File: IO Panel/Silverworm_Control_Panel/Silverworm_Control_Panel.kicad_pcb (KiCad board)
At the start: 2 copper layers, 74 x 208.7 mm, 32 parts, among them J1 Microfit 6-pin, J2 Conn_01x15, J3 Conn_01x15, J4 JST-PH-2PIN, J5 JST-PH-2PIN, J6 JST-PH-2PIN, J7 JST-PH-2PIN, SW1 SW_SPDT

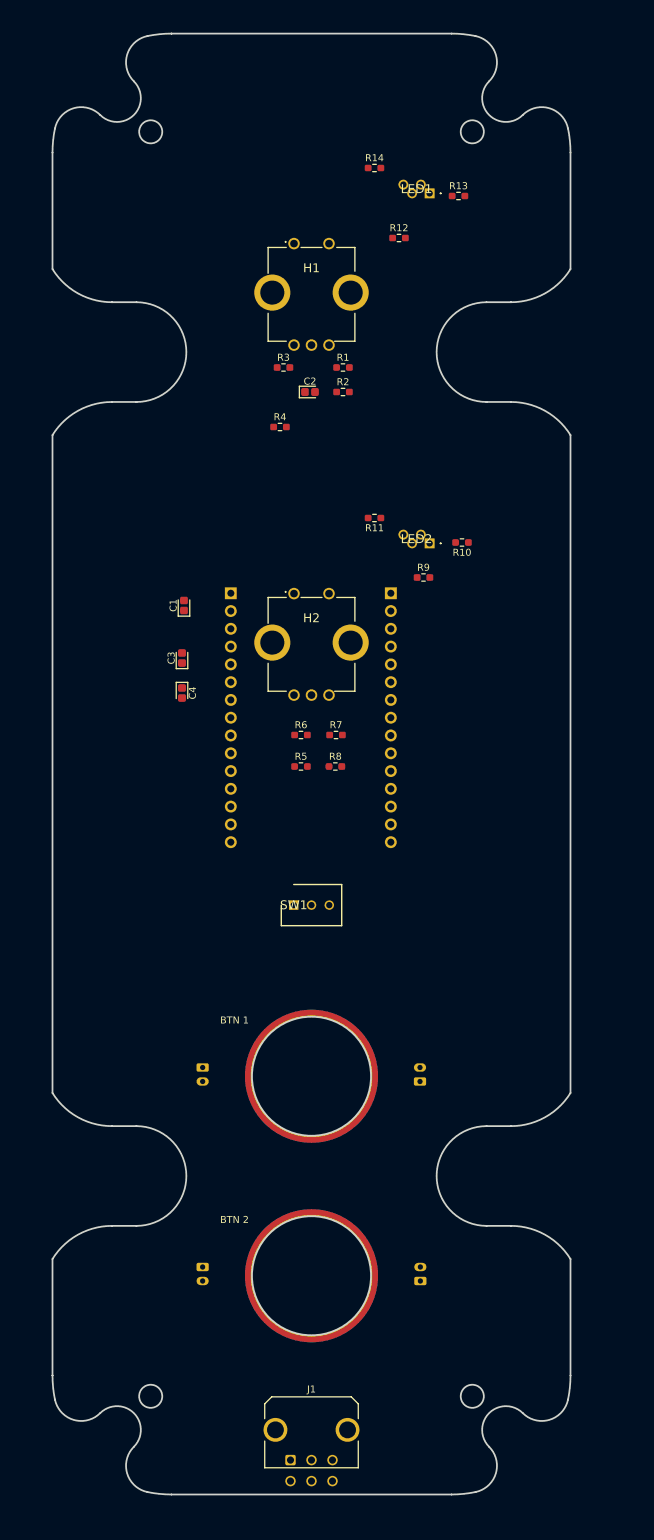
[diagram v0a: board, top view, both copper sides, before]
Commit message: Added footprints and board connectors
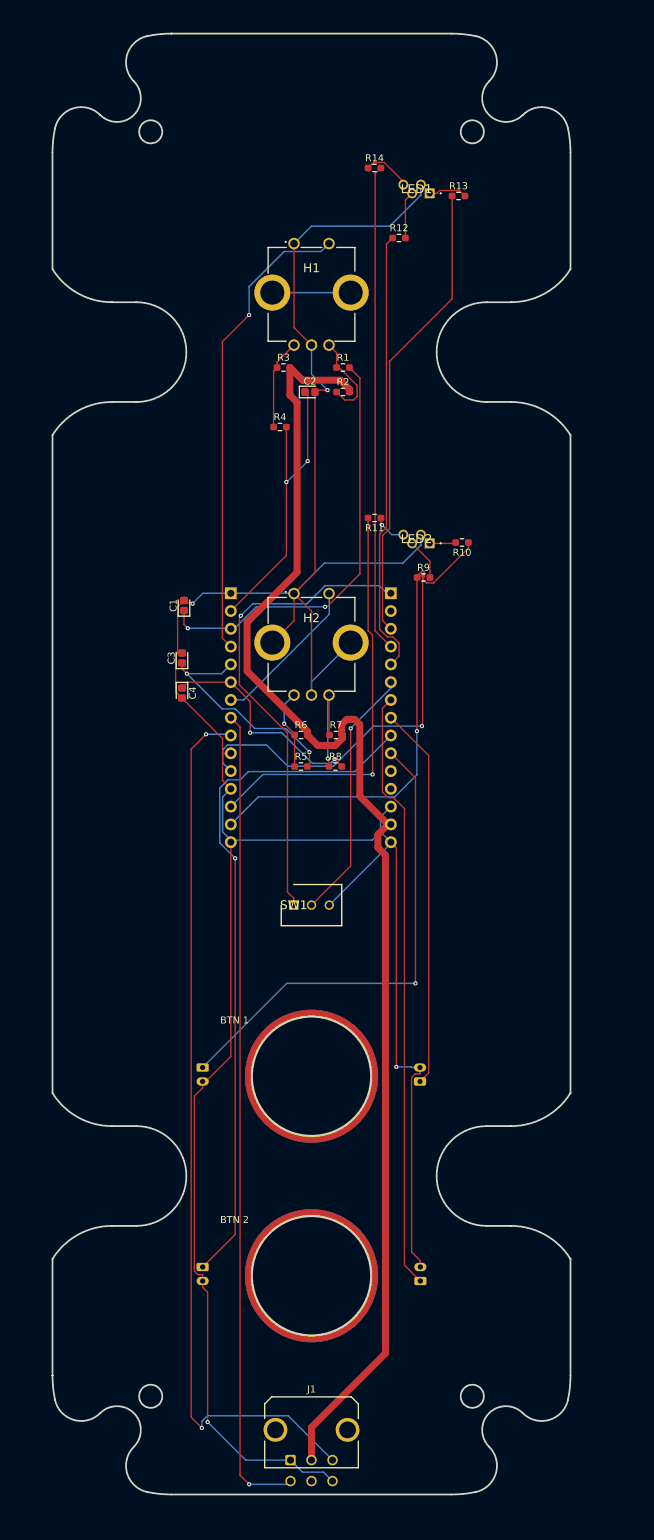
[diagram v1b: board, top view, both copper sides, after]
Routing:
- net GND: track 0.00 -> 420.0 mm, vias 0 -> 4
- net /5V0: track 0.00 -> 193.5 mm
- net /SCL: track 0.00 -> 126.8 mm, vias 0 -> 2
- net /SDA: track 0.00 -> 116.7 mm, vias 0 -> 1
- net /BTN2: track 0.00 -> 98.8 mm, vias 0 -> 1
- net /BTN2_LED: track 0.00 -> 86.2 mm
- net /BTN1: track 0.00 -> 69.7 mm, vias 0 -> 1
- net /LED1-G: track 0.00 -> 69.6 mm
- net /3V3: track 0.00 -> 68.3 mm, vias 0 -> 1
- net /LED2-R: track 0.00 -> 67.9 mm, vias 0 -> 1
- net /Dial1NO: track 0.00 -> 67.5 mm, vias 0 -> 1
- net /LED1-R: track 0.00 -> 66.4 mm
- net /LED1-B: track 0.00 -> 63.8 mm
- net /LED2-B: track 0.00 -> 60.9 mm, vias 0 -> 1
- net /Dial1B: track 0.00 -> 60.8 mm, vias 0 -> 2
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
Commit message: Added 3d molex connector to UI panel
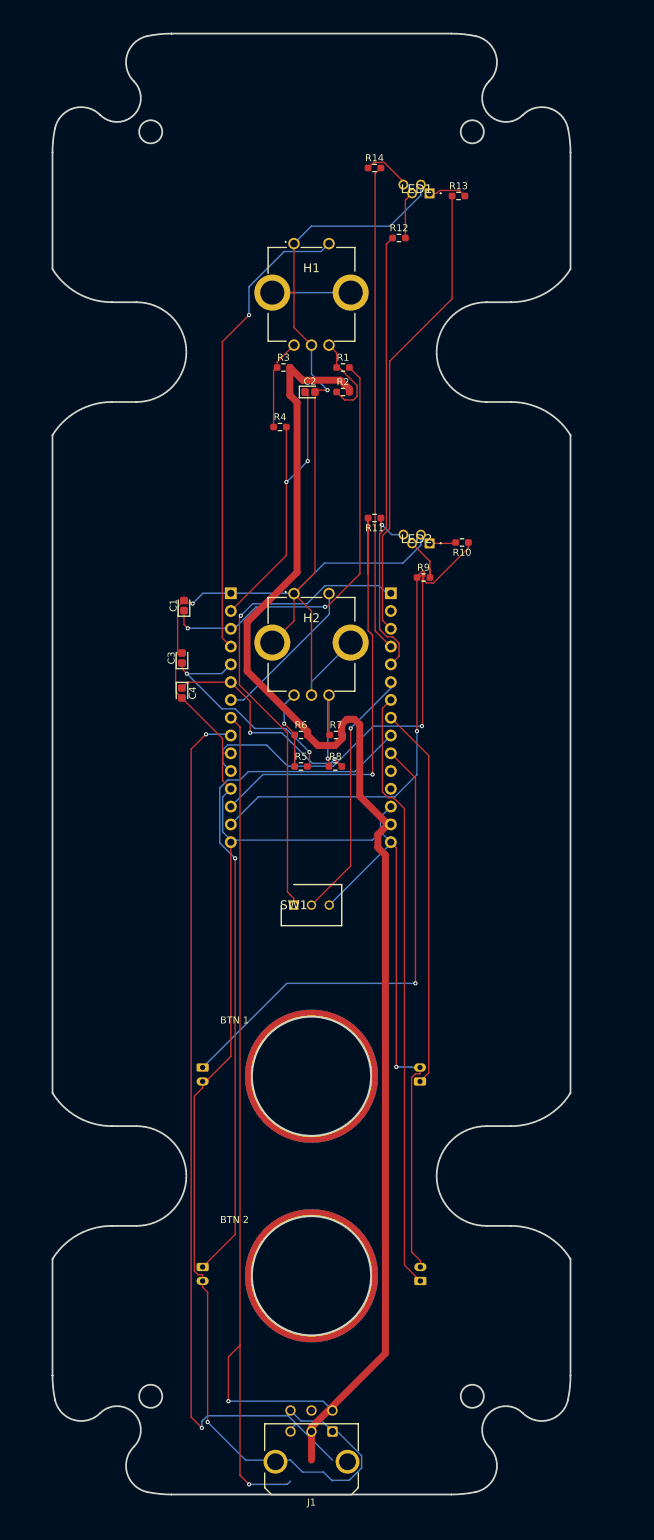
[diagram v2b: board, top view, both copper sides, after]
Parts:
- moved J1 7.26 mm to (153.0, 261.0), turned to 180 degrees
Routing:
- net /SDA: track 116.7 -> 140.8 mm, vias 1 -> 2
- net GND: track 420.0 -> 439.6 mm
- net /LED2-G: track 59.1 -> 67.1 mm
- net Net-(H2-CHANNEL_A): track 11.4 -> 13.6 mm
- net /SCL: track 126.8 -> 128.2 mm
- net Net-(LED2-A_B): track 5.93 -> 7.10 mm

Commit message: Layout and IO edits
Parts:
- J1: moved to B.Cu
- moved J1 6.00 mm to (147.0, 261.0), turned to 0 degrees

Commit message: control panel etc data
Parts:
- removed BTN 1: MountingHole_17mm_Pad_TopBottom, CustomLibrary:MountingHole_17mm_Pad_TopBottom
- removed BTN 2: MountingHole_17mm_Pad_TopBottom, CustomLibrary:MountingHole_17mm_Pad_TopBottom
- removed J6, J7: JST-PH-2PIN, Connector_JST:JST_PH_B2B-PH-K_1x02_P2.00mm_Vertical
- added H3: MountingHole, CustomLibrary:MountingHole_17mm_Pad_TopBottom, F.Cu at (150.0, 210.5)
- J4, J5: value JST-PH-2PIN -> JST-XH-2PIN
- moved R1 14.4 mm to (151.0, 123.0), turned to 180 degrees
- moved C2 14.4 mm to (140.0, 123.0), turned to 180 degrees
- moved R6 8.36 mm to (146.1, 169.5), turned to 180 degrees
- moved R4 5.50 mm to (145.5, 123.0), turned to 180 degrees
- moved R8 3.56 mm to (154.1, 169.5), turned to 180 degrees
- moved R7 3.55 mm to (154.1, 165.0), turned to 180 degrees
- moved R3 3.54 mm to (145.5, 112.5)
- moved R2 3.41 mm to (151.1, 112.5), turned to 180 degrees
- moved C1 3.26 mm to (130.5, 146.0), turned to 180 degrees
- moved R5 2.61 mm to (146.1, 165.0), turned to 180 degrees
- moved J5 2.07 mm to (164.9, 209.0), turned to -90 degrees
- moved C3 1.41 mm to (130.5, 151.5), turned to 180 degrees
- moved C4 1.41 mm to (130.5, 156.5), turned to 180 degrees
- moved LED2 0.18 mm to (167.0, 134.0)
- turned R13 to 180 degrees
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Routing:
- net GND: track 439.6 -> 0.00 mm, vias 4 -> 0
- net /5V0: track 193.5 -> 25.9 mm, vias 0 -> 2
- net /BTN2: track 98.8 -> 0.00 mm, vias 1 -> 0
- net /BTN2_LED: track 86.2 -> 0.00 mm
- net /LED2-B: track 60.9 -> 127.5 mm, vias 1 -> 2
- net /LED1-B: track 63.8 -> 128.4 mm
- net /LED1-G: track 69.6 -> 106.8 mm
- net /LED2-R: track 68.3 -> 105.3 mm, vias 1 -> 2
- net /Dial1NO: track 67.5 -> 100.1 mm, vias 1 -> 0
- net /SDA: track 140.8 -> 115.5 mm, vias 2 -> 0
- net /Dial1B: track 60.8 -> 35.8 mm, vias 2 -> 0
- net /Dial2B: track 31.6 -> 50.0 mm, vias 2 -> 0
- net /Dial1A: track 43.9 -> 28.3 mm, vias 2 -> 0
- net /TOGGLE: track 36.5 -> 51.2 mm, vias 1 -> 0
- net /LED1-R: track 66.4 -> 80.6 mm
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- added copper zone on B.Cu, net /5V0
- added copper zone on F.Cu, net GND
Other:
- board text added: "Button"
- board text added: "LED"
- board text added: "Put solder here please :)"
- board text added: "Silverworm Control Panel Board Designed by Zak Leek © Zak Leek, Imperial College London, 2026"
- board text added: "Waveshare ESP32-H2 Development Board"

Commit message: conytrol panel
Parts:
- added TP1: 5V0 Testpoint, TestPoint:TestPoint_THTPad_D2.5mm_Drill1.2mm, F.Cu at (146.0, 243.0)
- added TP2: GND Testpoint, TestPoint:TestPoint_Pad_D3.0mm, F.Cu at (160.0, 243.0)
- added TP3: 3V3 Testpoint, TestPoint:TestPoint_THTPad_D2.5mm_Drill1.2mm, F.Cu at (154.0, 196.0)
- C1, C2, C3, C4: footprint Capacitor_Tantalum_SMD:CP_EIA-1608-10_AVX-L -> Capacitor_SMD:C_0805_2012Metric_Pad1.18x1.45mm_HandSolder
- LED1, LED2: value MP008267 -> MP008267 zl edit; footprint MP008267_LED:MP008267 -> MP008267_LED:MP008267 zl edit
- R1, R10, R11, R12, R13, R14, R2, R3, R4, R5, R6, R7, R8, R9: footprint Resistor_SMD:R_0603_1608Metric_Pad0.98x0.95mm_HandSolder -> Resistor_SMD:R_0805_2012Metric_Pad1.20x1.40mm_HandSolder
- moved C1 1.00 mm to (130.5, 145.0)
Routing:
- net GND: track 0.00 -> 22.8 mm, vias 0 -> 2
- net /3V3: track 79.5 -> 94.6 mm
- net /LED1-B: track 128.4 -> 139.8 mm
- net /LED1-G: track 106.8 -> 117.9 mm
- net /LED2-G: track 72.5 -> 75.8 mm
- net /LED2-B: track 127.5 -> 130.4 mm
- net /LED2-R: track 105.3 -> 108.0 mm
- net /Dial1B: track 35.8 -> 37.4 mm
- net /SDA: track 115.5 -> 116.3 mm
- net Net-(LED2-A_B): track 6.00 -> 5.50 mm
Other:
- outline, holes or cut-outs redrawn

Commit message: finalised motherboard
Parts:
- moved TP1 17.7 mm to (163.0, 238.0)
- moved TP2 6.71 mm to (163.0, 249.0)
